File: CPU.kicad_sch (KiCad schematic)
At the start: 31 parts, among them U12 RP2A03 CPU, U13 SST39SF040-70-4C-NHE, U14 74HC139, U17 TLV863MDBZR, U3 IS62C256AL-45TLI

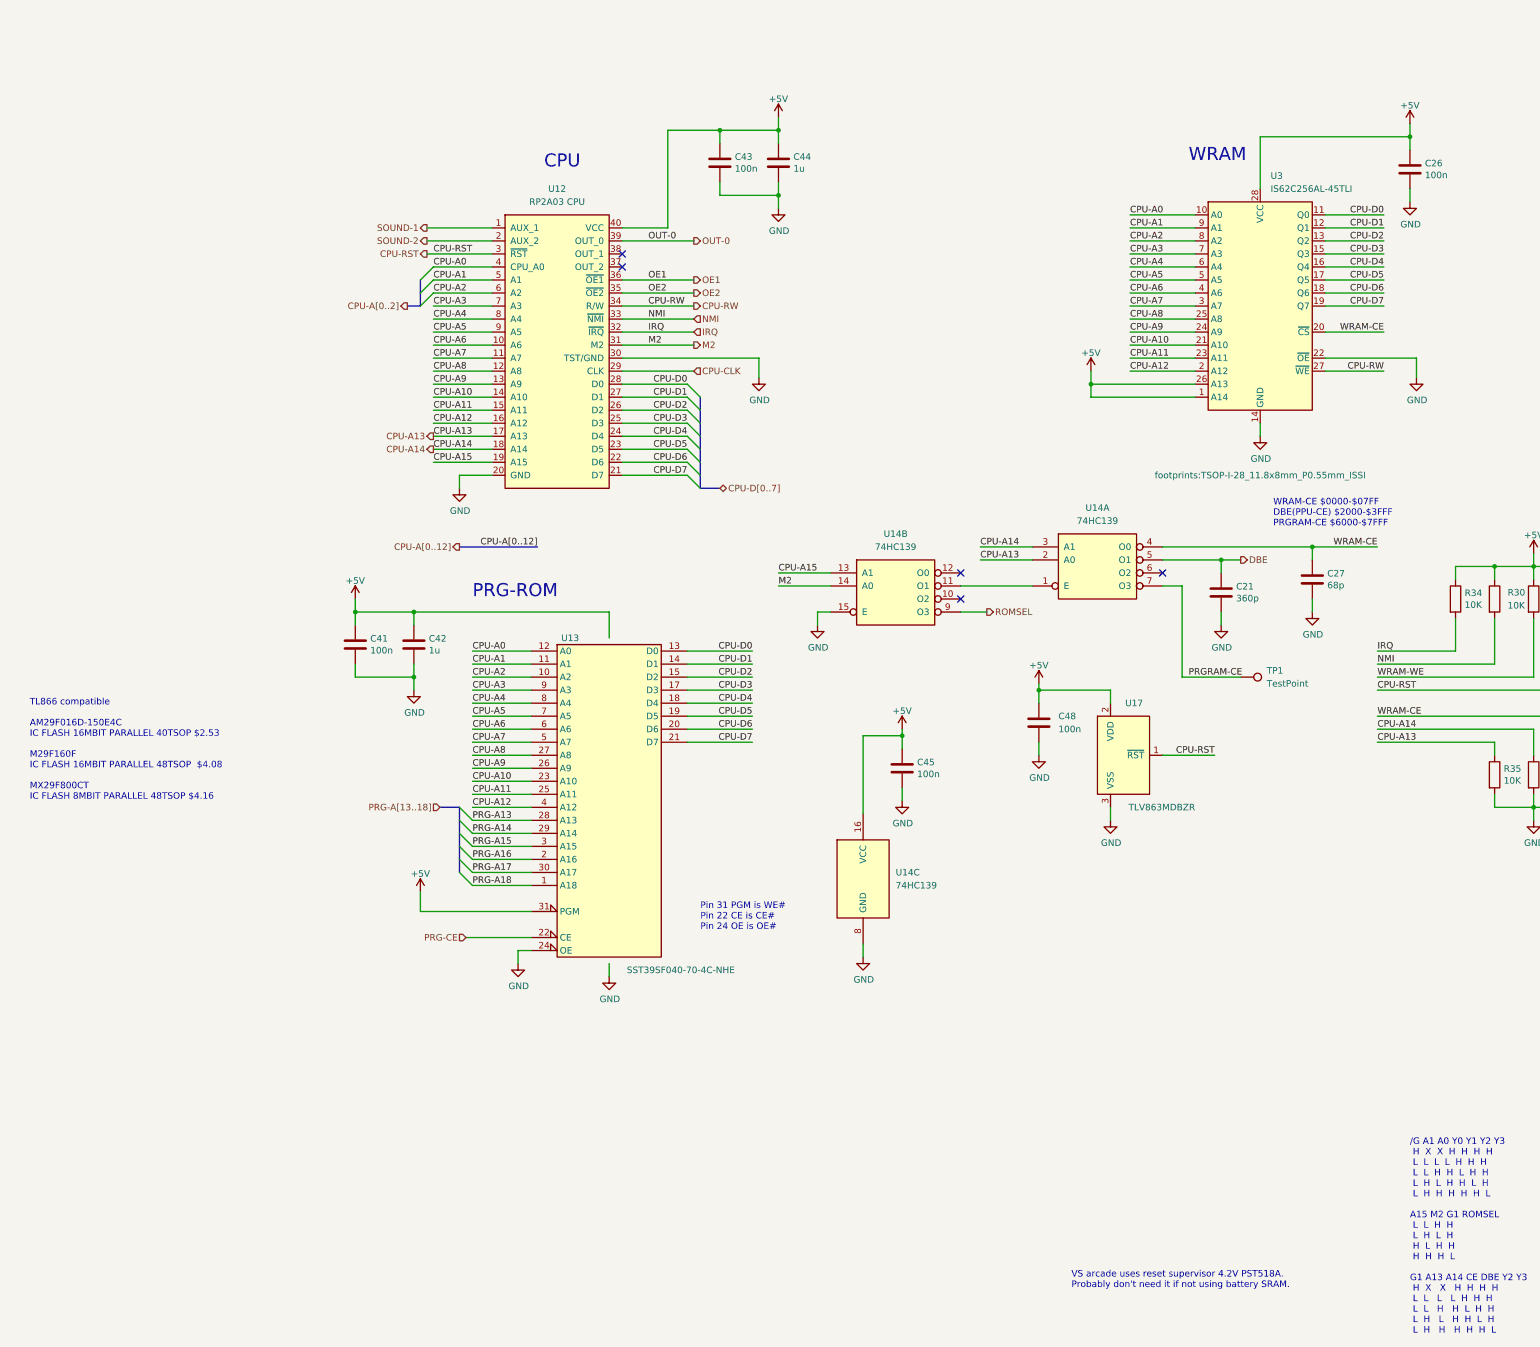
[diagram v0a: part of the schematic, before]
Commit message: rev2 sent to fab
Added CHR RAM.
Changed board to 4 layers (was 2 layers).
Changed passives to 0603 (was 0402)
Fixed CIRAM-A10 not being hooked up
Fixed PPU-A10..A12 being hooked to VRAM but should have been.
Added more silkscreen for easier debugging.
Added filter inductor to 5V from USB-C.
Changed video out to stock (was THS7374)
Changed audio circuit to stock (was headphone amp IC)
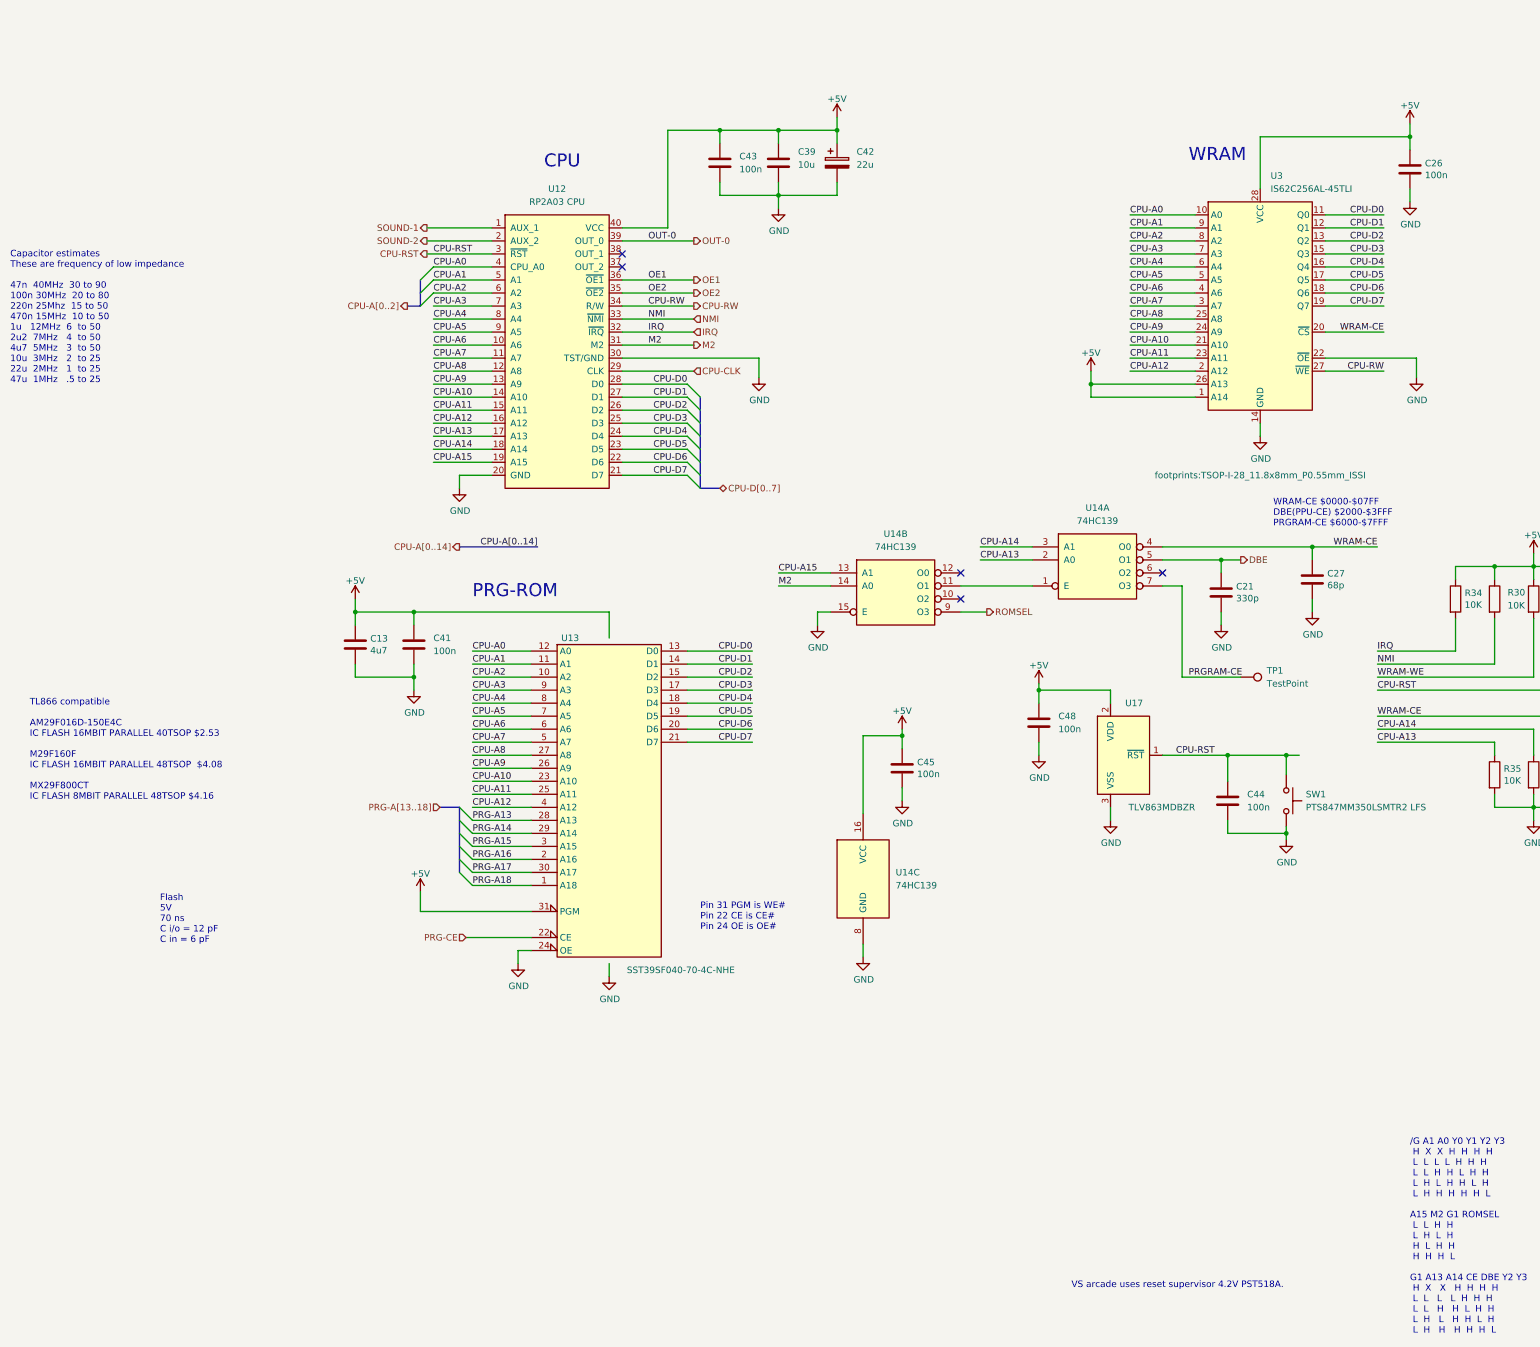
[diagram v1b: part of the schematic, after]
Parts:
- removed C42: 1u, Capacitor_SMD:C_0402_1005Metric, symbol Device:C
- added C13: 4u7, Capacitor_SMD:C_0805_2012Metric_Pad1.18x1.45mm_HandSolder, symbol Device:C
- added C39: 10u, Capacitor_SMD:C_1206_3216Metric_Pad1.33x1.80mm_HandSolder, symbol Device:C
- added C42: 22u, Capacitor_Tantalum_SMD:CP_EIA-3216-18_Kemet-A_Pad1.58x1.35mm_HandSolder, symbol Device:C_Polarized
- added SW1: PTS847MM350LSMTR2 LFS, footprints:SW_SPST_PTS847, symbol Switch:SW_Push
- C21: value 360p -> 330p; footprint Capacitor_SMD:C_0603_1608Metric -> Capacitor_SMD:C_0603_1608Metric_Pad1.08x0.95mm_HandSolder; Digikey 399-15397-1-ND -> (none); MPN C0603C361J5GAC7867 -> (none)
- C26, C41, C43, C45, C48: footprint Capacitor_SMD:C_0402_1005Metric -> Capacitor_SMD:C_0603_1608Metric_Pad1.08x0.95mm_HandSolder; Digikey 1276-1509-2-ND -> (none); MPN CL05B104KO5NNWC -> (none); QOH 10000 -> (none)
- C27: footprint Capacitor_SMD:C_0402_1005Metric -> Capacitor_SMD:C_0603_1608Metric_Pad1.08x0.95mm_HandSolder; Digikey 311-1340-1-ND -> (none); MPN CC0402JRNPO9BN680 -> (none)
- C44: value 1u -> 100n; footprint Capacitor_SMD:C_0402_1005Metric -> Capacitor_SMD:C_0603_1608Metric_Pad1.08x0.95mm_HandSolder; Digikey 490-3890-2-ND -> (none); MPN GRM155R61A105KE15D -> (none); Size 0402 -> (none)
- R10, R30, R34, R35, R37: footprint Resistor_SMD:R_0402_1005Metric -> Resistor_SMD:R_0603_1608Metric_Pad0.98x0.95mm_HandSolder; Digikey P10.0KLCT-ND -> (none); MPN ERJ-2RKF1002X -> (none); QOH 5000 -> (none)
- R36: footprint Resistor_SMD:R_0402_1005Metric -> Resistor_SMD:R_0603_1608Metric_Pad0.98x0.95mm_HandSolder; Digikey 311-27KJRCT-ND -> (none); MPN RC0402JR-0727KL -> (none)
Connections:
- net +5V: now also C13.2, C39.1, C42.1; no longer C44.2
- net CPU-RST: now also C44.2, SW1.2
- net GND: now also C13.1, C39.2, C42.2, SW1.1
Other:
- note added: "Capacitor estimates These are frequency of low impedance 47n 40MHz 30 to 90 100n 30MHz 20 to 80 220n 25Mhz 15 to 50 470n 15MHz 10 to 50 1u 12MHz 6 to 50 2u2 7MHz 4 to 50 4u7 5MHz 3 to 50 10u 3MHz 2 to 25 22u 2MHz 1 to 25 47u 1MHz .5 to 25"
- note added: "Flash 5V 70 ns C i/o = 12 pF C in = 6 pF"
- note added: "VS arcade uses reset supervisor 4.2V PST518A."
- note removed: "VS arcade uses reset supervisor 4.2V PST518A. Probably don't need it if not using battery SRAM."
- moved on the sheet: C41

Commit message: filled out BOM
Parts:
- removed #C3, #C48: 100n, Capacitor_SMD:C_0402_1005Metric, symbol Device:C
- removed #R9: 10K, Resistor_SMD:R_0402_1005Metric, symbol Device:R
- removed #U10: IS62C256AL-45TLI, footprints:TSOP-I-28_11.8x8mm_P0.55mm_ISSI, symbol Memory_RAM:KM62256CLP
- removed #U11, #U4: 74HC00, symbol 74xx:74HC00
- removed #U2: FM18W08-SG, footprints:SOIC-28W_7.5_8.7mm, symbol Memory_NVRAM:FM18W08-SG
- removed #U3: 74HC04, symbol 74xx:74HC04
- removed #U8: 74AHC04, symbol 74xx:74AHC04
- C13: Digikey (none) -> 1276-1244-1-ND; MPN (none) -> CL21A475KAQNNNE
- C21: Digikey (none) -> 399-C0603C331J5GAC7867CT-ND; MPN (none) -> C0603C331J5GAC7867
- C26, C41, C43, C44, C45, C48: Digikey (none) -> 1276-CL10B104KB8WPNDCT-ND; MPN (none) -> CL10B104KB8WPND
- C27: Digikey (none) -> 399-C0603C680J5GAC7867CT-ND; MPN (none) -> C0603C680J5GAC7867
- C39: Digikey (none) -> 1276-1075-1-ND; MPN (none) -> CL31A106KAHNNNE
- C42: Digikey (none) -> 478-1663-1-ND; MPN (none) -> TAJA226K010RNJ
- R10, R30, R34, R35, R37: Digikey (none) -> RMCF0603FT10K0CT-ND; MPN (none) -> RMCF0603FT10K0
- R36: Digikey (none) -> RMCF0603FT27K0CT-ND; MPN (none) -> RMCF0603FT27K0
- SW1: Digikey (none) -> 108-PTS847MM350LSMTR2LFSCT-ND; MPN (none) -> PTS847MM350LSMTR2 LFS
- TP1: now left out of the parts list
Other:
- note removed: "MMC3 schematic PRG_RAM_+CE high when CPU $6000-$7FFF and PRG RAM enabled"
- note removed: "PRG RAM MMC3 = WRAM-CE2 SNROM = CHR-A16"
- note removed: "PRG-RAM"
- note removed: "pin 1 /CLR sets all four outputs low reguardless of CLK or LOAD pin 2 CLK pin 9 /LOAD"
